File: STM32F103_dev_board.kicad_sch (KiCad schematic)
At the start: 33 parts, among them IC1 TLV70233DBVR, J1 Conn_ARM_JTAG_SWD_20, J2 Conn_01x20_Pin, J3 Conn_01x20_Pin, J4 Conn_02x03_Odd_Even, J5 USB_C_Receptacle, U1 STM32F103RBTx, U4 FT232RL, Y1 8MHz, Y2 Crystal_GND23

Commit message: Changed USB C connector and fixed wiring to FT232RL
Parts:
- removed J5: USB_C_Receptacle, Connector_USB:USB_C_Receptacle_Molex_105450-0101, symbol Connector:USB_C_Receptacle
- removed R8: 20, Resistor_SMD:R_0201_0603Metric, symbol Device:R
- added J6: USB4800-03-A, SamacSys_Parts:USB480003A_BIGPAD, symbol SamacSys_Parts:USB4800-03-A
- added R1: 5.1k, Resistor_SMD:R_0201_0603Metric, symbol Device:R
- R3: value 5.1k -> 20
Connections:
- net 5V: now also J6.A4 (VBUS_1), J6.A9 (VBUS_2)
- net GND: now also R2.1, J6.A1 (GND_1), J6.A12 (GND_2), J6.MH3, J6.MH4, J6.MH5, J6.MH6, R1.1; no longer R2.2, R3.2
- net PA10/USART1_RX: no longer U4.5 (RXD)
- net PA9/USART1_TX: now also U4.5 (RXD)
- net USBDM: now also R7.2; no longer R7.1
- net USBDP: now also R3.2
- net at R3.1: now also J6.A6 (DP1)
- new net: J6.A5 (CC1), R2.2
- new net: J6.A7 (DN1), R7.1
- new net: J6.B5 (CC2), R1.2

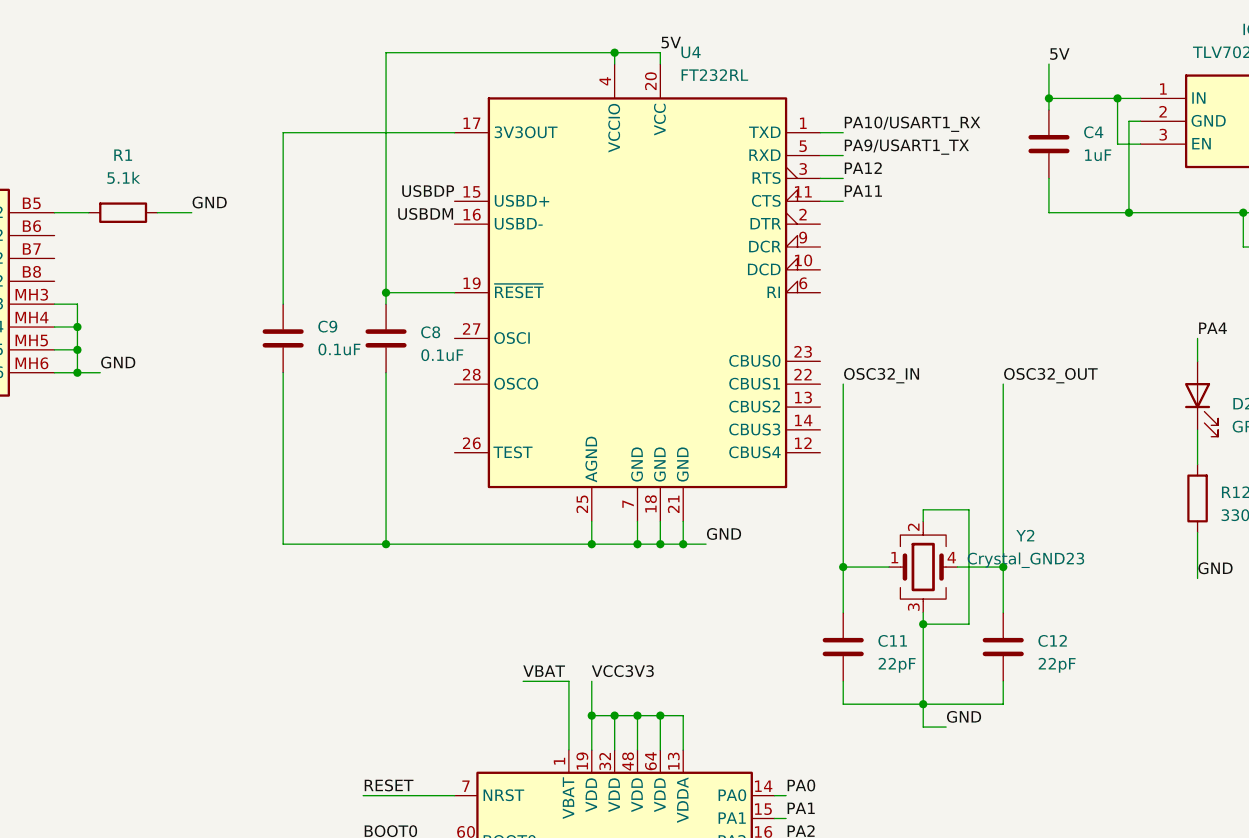
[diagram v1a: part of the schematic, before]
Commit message: Changed FT232RL into FT232RNL, fixed 32.768kHz crystal load capacitor
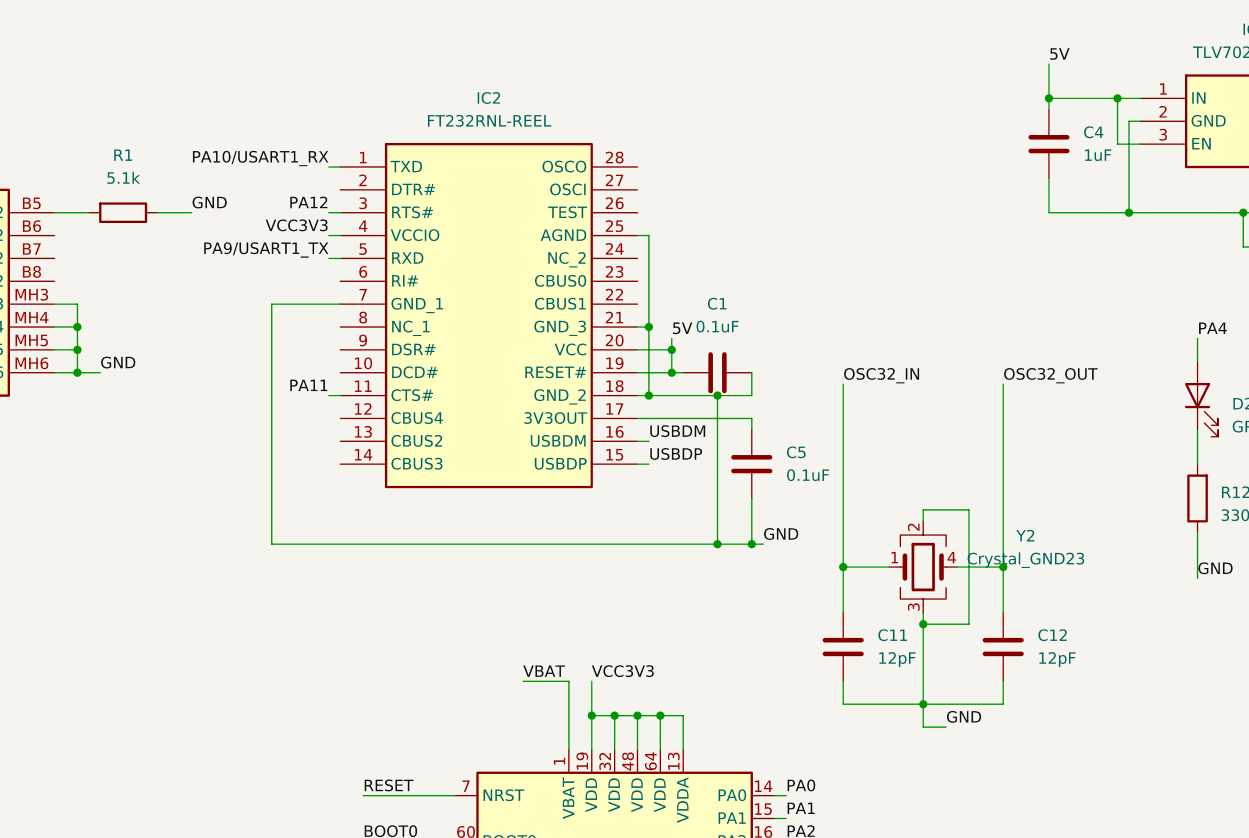
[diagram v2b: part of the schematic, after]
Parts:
- removed C8, C9: 0.1uF, Capacitor_SMD:C_0201_0603Metric, symbol Device:C
- removed U4: FT232RL, Package_SO:SSOP-28_5.3x10.2mm_P0.65mm, symbol Interface_USB:FT232RL
- added C1, C5: 0.1uF, Capacitor_SMD:C_0201_0603Metric, symbol Device:C
- added IC2: FT232RNL-REEL, SOP65P780X200-28N, symbol SamacSys_Parts:FT232RNL-REEL
- C11, C12: value 22pF -> 12pF
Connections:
- net 5V: now also C1.2, IC2.19 (RESET#), IC2.20 (VCC)
- net GND: now also C1.1, C5.1, IC2.18 (GND_2), IC2.21 (GND_3), IC2.25 (AGND), IC2.7 (GND_1)
- net PA10/USART1_RX: now also IC2.1 (TXD)
- net PA11: now also IC2.11 (CTS#)
- net PA12: now also IC2.3 (RTS#)
- net PA9/USART1_TX: now also IC2.5 (RXD)
- net RESET: now also IC2.4 (VCCIO)
- net USBDM: now also IC2.16 (USBDM)
- net USBDP: now also IC2.15 (USBDP)
- new net: C5.2, IC2.17 (3V3OUT)

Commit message: Updated production files
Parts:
- J6: footprint SamacSys_Parts:USB480003A_BIGPAD -> SamacSys_Parts:USB480003A
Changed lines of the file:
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@@
       (effects (font (size 1.27 1.27)))
     )
-    (property "Footprint" "SamacSys_Parts:USB480003A_BIGPAD" (at 66.04 130.48 0)
+    (property "Footprint" "SamacSys_Parts:USB480003A" (at 66.04 130.48 0)
       (effects (font (size 1.27 1.27)) (justify left top) hide)
     )
